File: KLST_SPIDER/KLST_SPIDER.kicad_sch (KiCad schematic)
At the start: 11 parts, among them J1 MIDI_IN, J2 MIDI_OUT, J3 UART, U1 H11L1

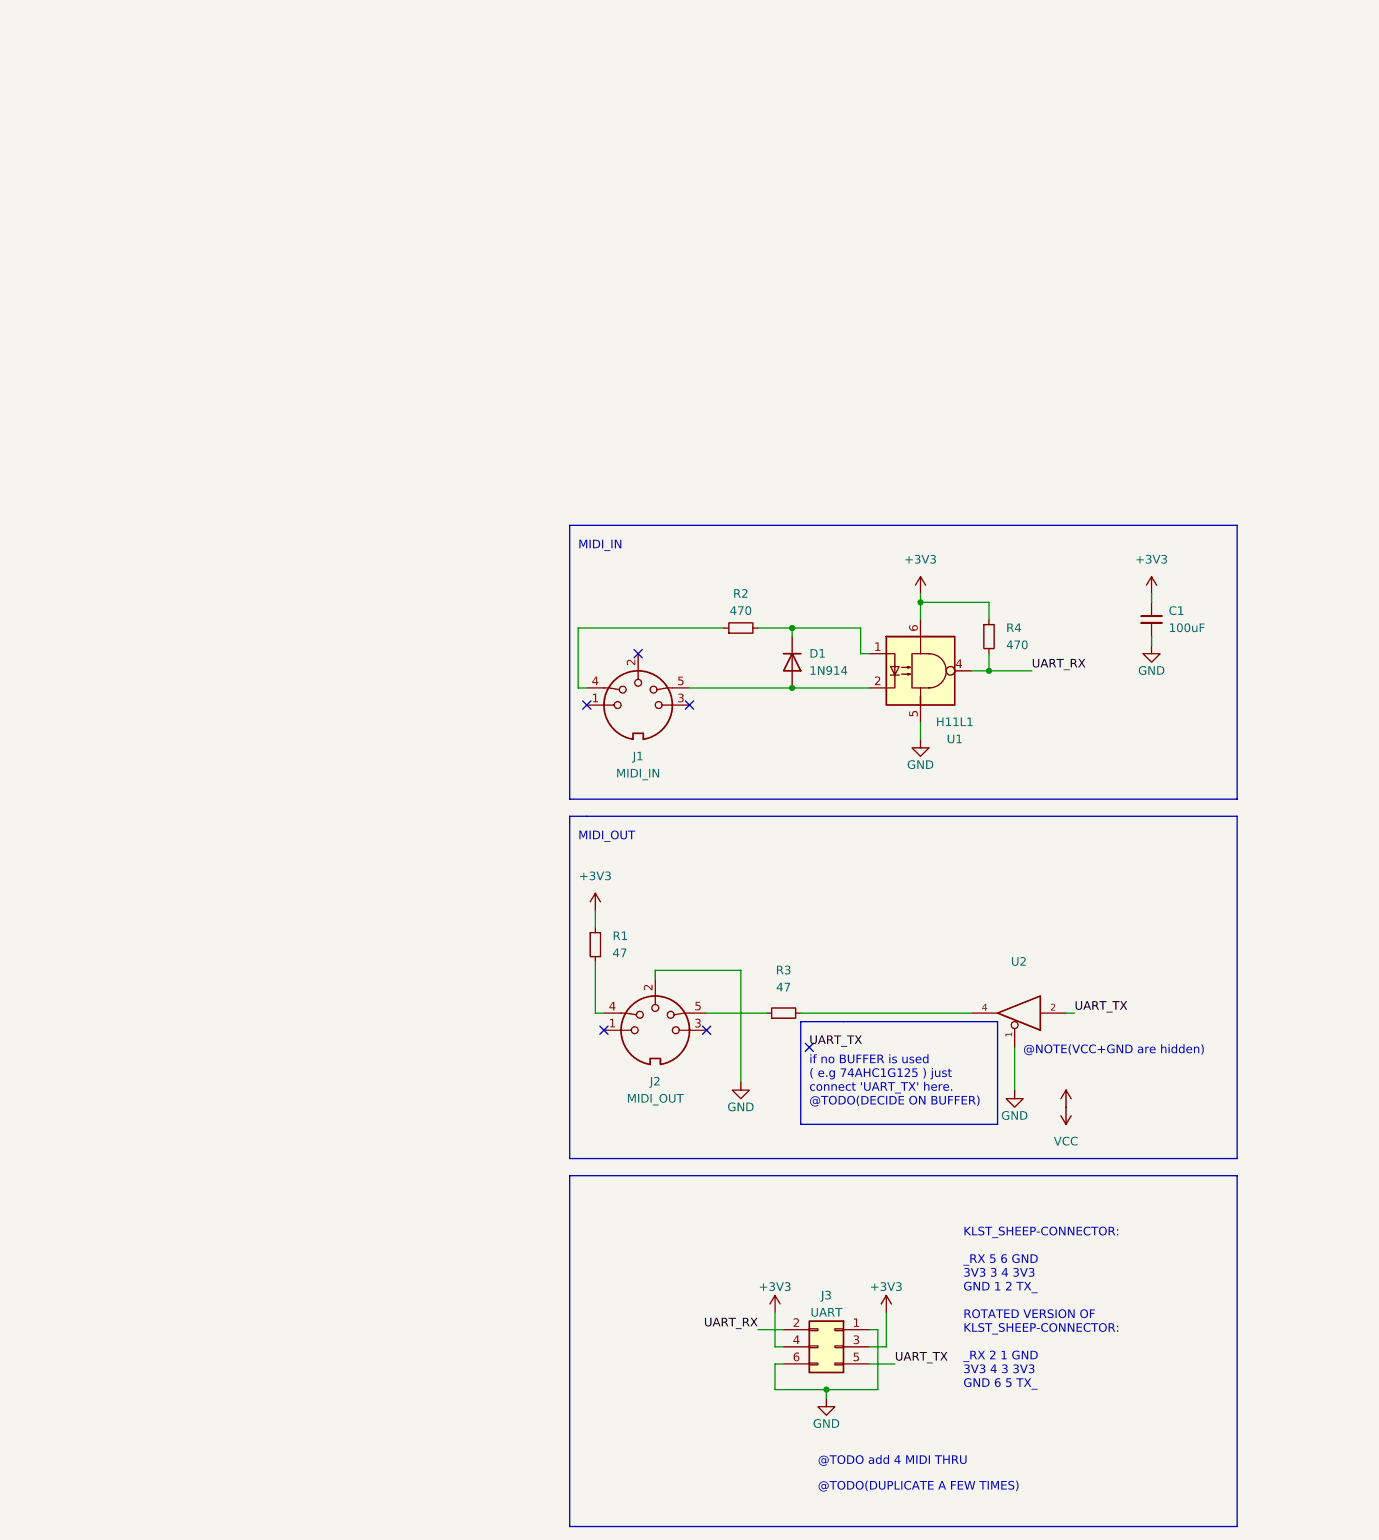
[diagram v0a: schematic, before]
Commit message: added connectors, created round PCB
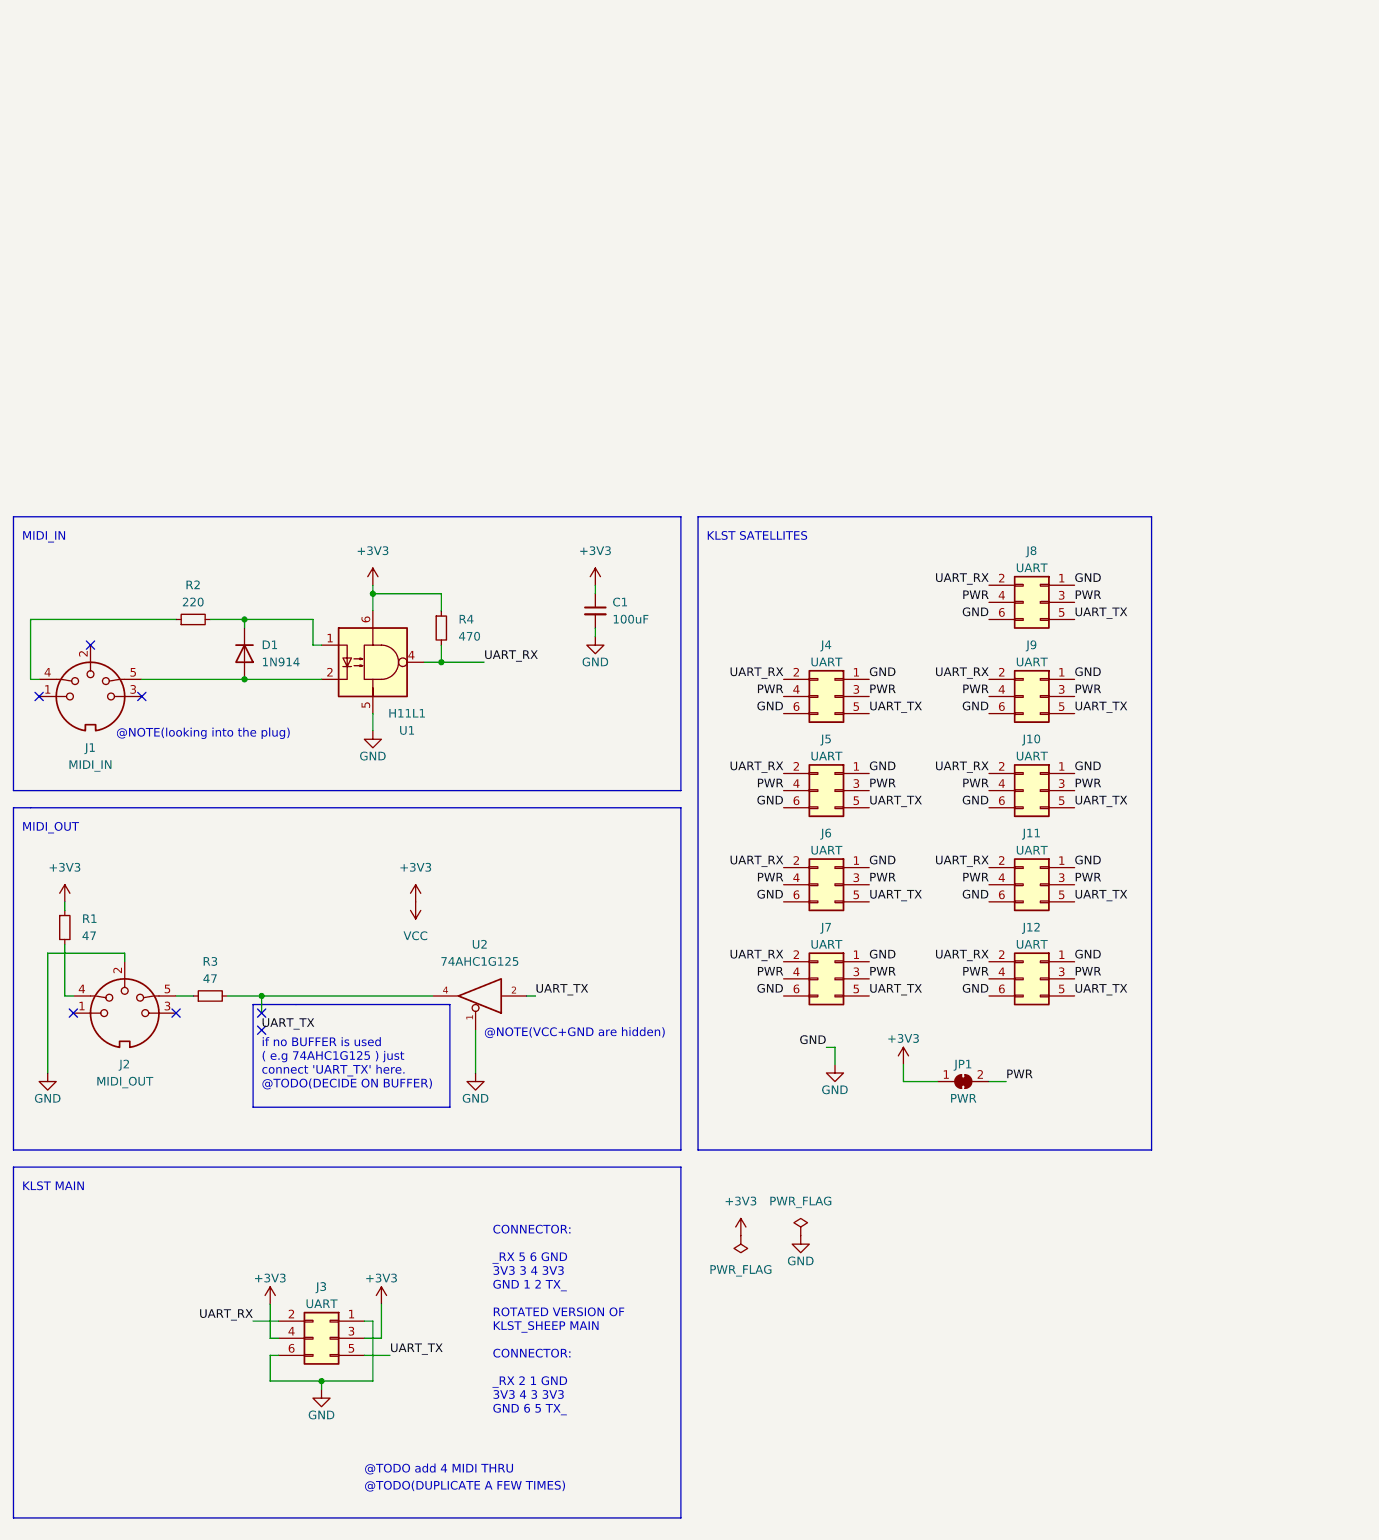
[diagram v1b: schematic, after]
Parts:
- added J10, J11, J12, J4, J5, J6, J7, J8, J9: UART, Connector_IDC:IDC-Header_2x03_P2.54mm_Horizontal, symbol Connector_Generic:Conn_02x03_Odd_Even
- added JP1: PWR, Jumper:SolderJumper-2_P1.3mm_Bridged_RoundedPad1.0x1.5mm, symbol Jumper:SolderJumper_2_Bridged
- C1: footprint (none) -> Capacitor_SMD:C_0805_2012Metric_Pad1.18x1.45mm_HandSolder
- R1, R3, R4: footprint Resistor_THT:R_Axial_DIN0207_L6.3mm_D2.5mm_P7.62mm_Horizontal -> Resistor_SMD:R_0805_2012Metric_Pad1.20x1.40mm_HandSolder
- R2: value 470 -> 220; footprint Resistor_THT:R_Axial_DIN0207_L6.3mm_D2.5mm_P7.62mm_Horizontal -> Resistor_SMD:R_0805_2012Metric_Pad1.20x1.40mm_HandSolder
- U1: footprint Package_DIP:DIP-6_W7.62mm -> Package_DIP:SMDIP-6_W9.53mm
- U2: value (none) -> 74AHC1G125; footprint (none) -> Package_TO_SOT_SMD:SOT-23-5_HandSoldering
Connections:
- net +3V3: now also JP1.1 (A)
- net GND: now also J10.1 (Pin_1), J10.6 (Pin_6), J11.1 (Pin_1), J11.6 (Pin_6), J12.1 (Pin_1), J12.6 (Pin_6), J4.1 (Pin_1), J4.6 (Pin_6), J5.1 (Pin_1), J5.6 (Pin_6), J6.1 (Pin_1), J6.6 (Pin_6), J7.1 (Pin_1), J7.6 (Pin_6), J8.1 (Pin_1), J8.6 (Pin_6), J9.1 (Pin_1), J9.6 (Pin_6)
- net UART_RX: now also J10.2 (Pin_2), J11.2 (Pin_2), J12.2 (Pin_2), J4.2 (Pin_2), J5.2 (Pin_2), J6.2 (Pin_2), J7.2 (Pin_2), J8.2 (Pin_2), J9.2 (Pin_2)
- net UART_TX: now also J10.5 (Pin_5), J11.5 (Pin_5), J12.5 (Pin_5), J4.5 (Pin_5), J5.5 (Pin_5), J6.5 (Pin_5), J7.5 (Pin_5), J8.5 (Pin_5), J9.5 (Pin_5)
- new net PWR: J10.3 (Pin_3), J10.4 (Pin_4), J11.3 (Pin_3), J11.4 (Pin_4), J12.3 (Pin_3), J12.4 (Pin_4), J4.3 (Pin_3), J4.4 (Pin_4), J5.3 (Pin_3), J5.4 (Pin_4), J6.3 (Pin_3), J6.4 (Pin_4), J7.3 (Pin_3), J7.4 (Pin_4), J8.3 (Pin_3), J8.4 (Pin_4), J9.3 (Pin_3), J9.4 (Pin_4), JP1.2 (B)
- no-connect marks 6 -> 7
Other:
- note added: "@NOTE(looking into the plug)"
- note added: "CONNECTOR: _RX 5 6 GND 3V3 3 4 3V3 GND 1 2 TX_ ROTATED VERSION OF KLST_SHEEP MAIN CONNECTOR: _RX 2 1 GND 3V3 4 3 3V3 GND 6 5 TX_"
- note added: "KLST MAIN"
- note added: "KLST SATELLITES"
- note removed: "KLST_SHEEP-CONNECTOR: _RX 5 6 GND 3V3 3 4 3V3 GND 1 2 TX_ ROTATED VERSION OF KLST_SHEEP-CONNECTOR: _RX 2 1 GND 3V3 4 3 3V3 GND 6 5 TX_"
- moved on the sheet: C1, D1, J1, J2, J3, R1, R2, R3, R4, U1, U2

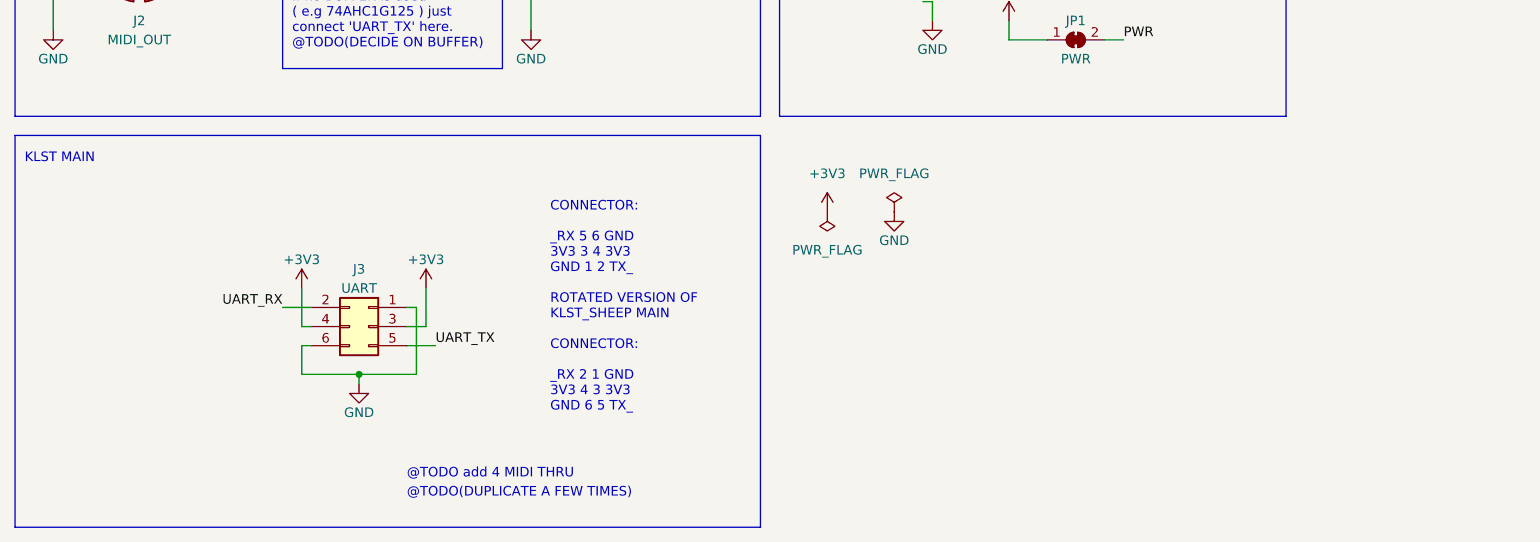
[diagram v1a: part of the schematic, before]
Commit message: added MIDI THRU
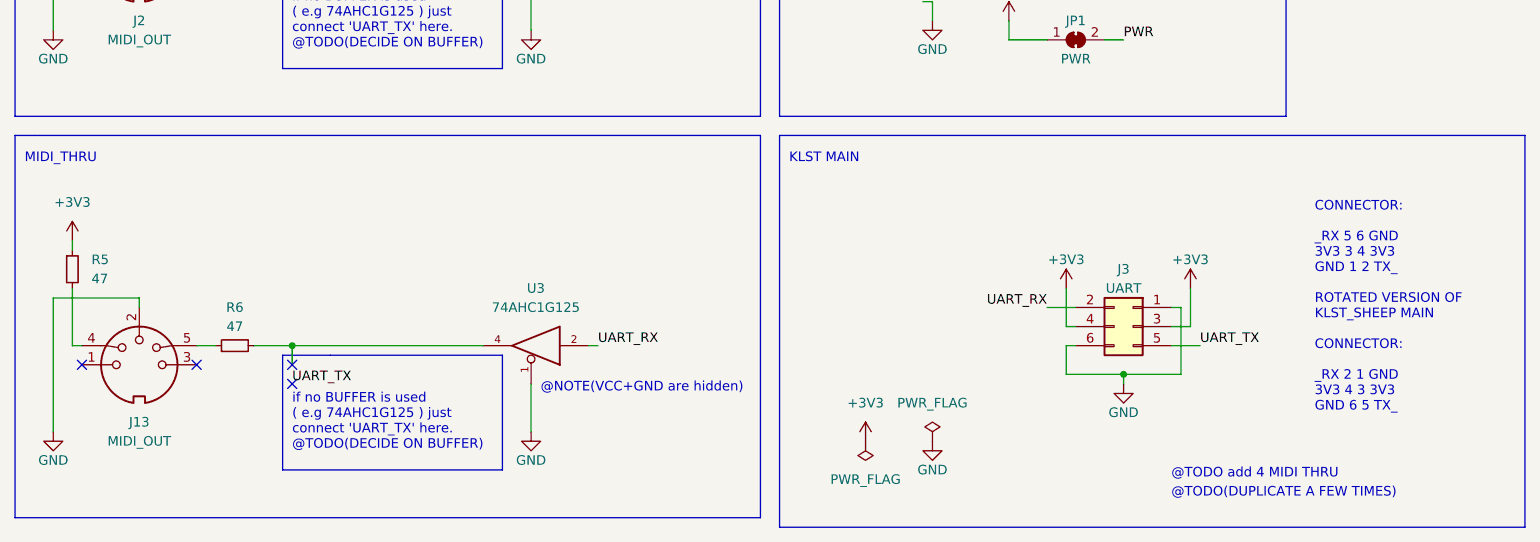
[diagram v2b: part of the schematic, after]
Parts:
- added J13: MIDI_OUT, DIN-5:DIN5-RA-PTH, symbol Connector:DIN-5_180degree
- added R5, R6: 47, Resistor_SMD:R_0805_2012Metric_Pad1.20x1.40mm_HandSolder, symbol Device:R_Small
- added U3: 74AHC1G125, Package_TO_SOT_SMD:SOT-23-5_HandSoldering, symbol 74xGxx:74AHC1G125
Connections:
- net +3V3: now also R5.1, U3.5 (VCC)
- net GND: now also J13.2, U3.1, U3.3 (GND)
- net UART_RX: now also U3.2
- new net: J13.4, R5.2
- new net: J13.5, R6.1
- new net: R6.2, U3.4
- no-connect marks 7 -> 11
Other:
- note added: "MIDI_THRU"
- moved on the sheet: J3
